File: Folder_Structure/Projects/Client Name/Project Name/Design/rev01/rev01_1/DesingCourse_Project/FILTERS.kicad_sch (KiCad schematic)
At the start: 17 parts, among them J10 874380643

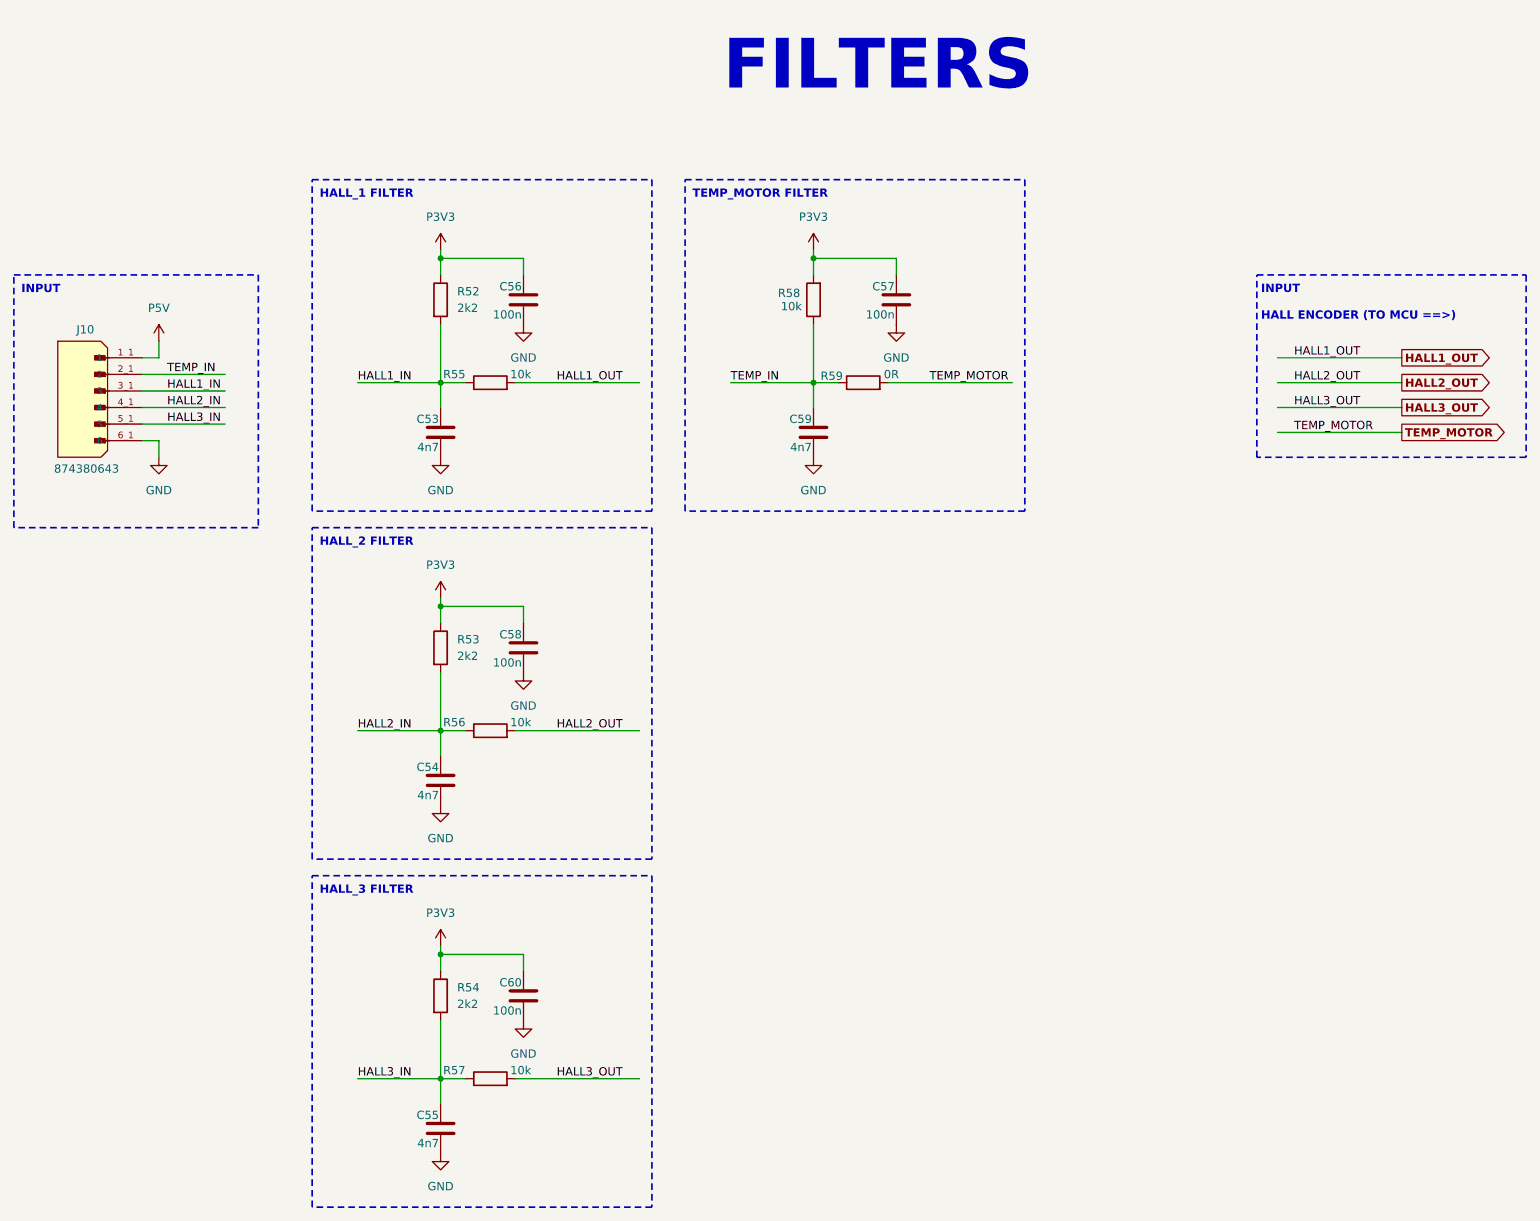
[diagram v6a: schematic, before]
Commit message: Update 16
Initial component placement done
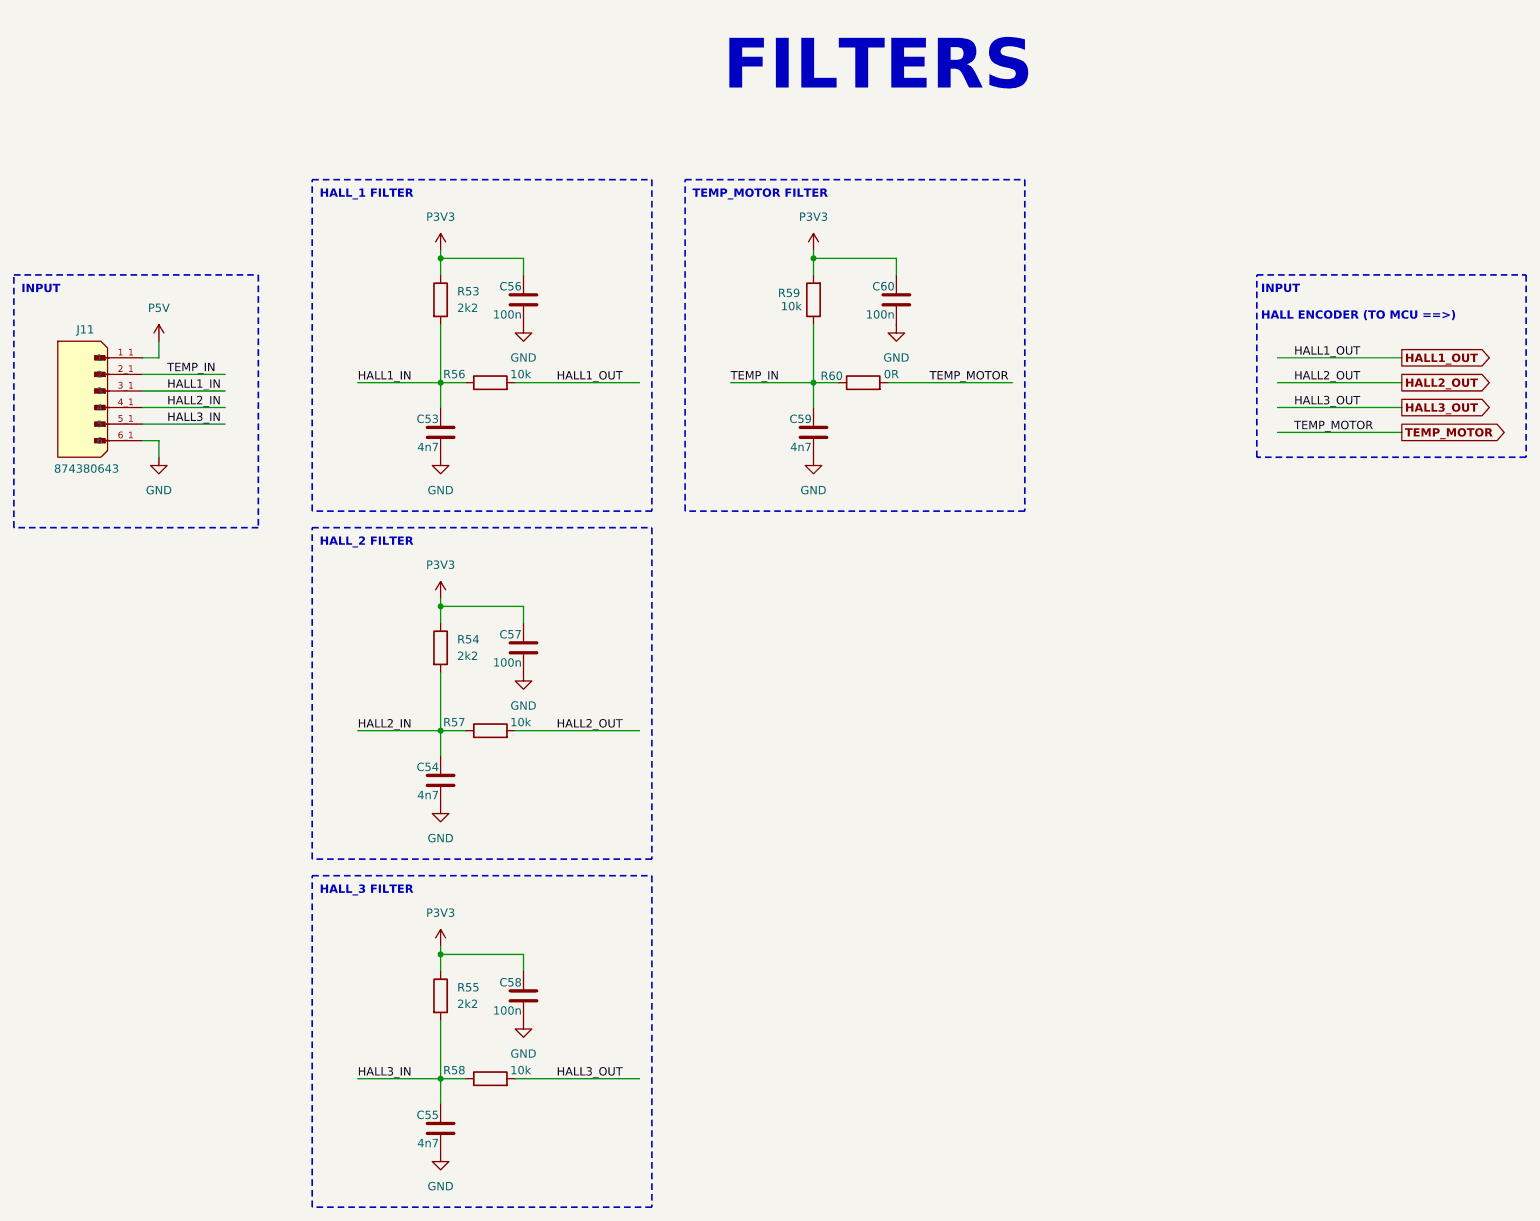
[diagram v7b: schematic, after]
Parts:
- renumbered C58 to C57, C60 to C58, C57 to C60, J10 to J11, R52 to R53, R53 to R54, R54 to R55, R55 to R56, R56 to R57, R57 to R58, R58 to R59, R59 to R60

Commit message: Update18
Layout finished, clean up or layout and designators.
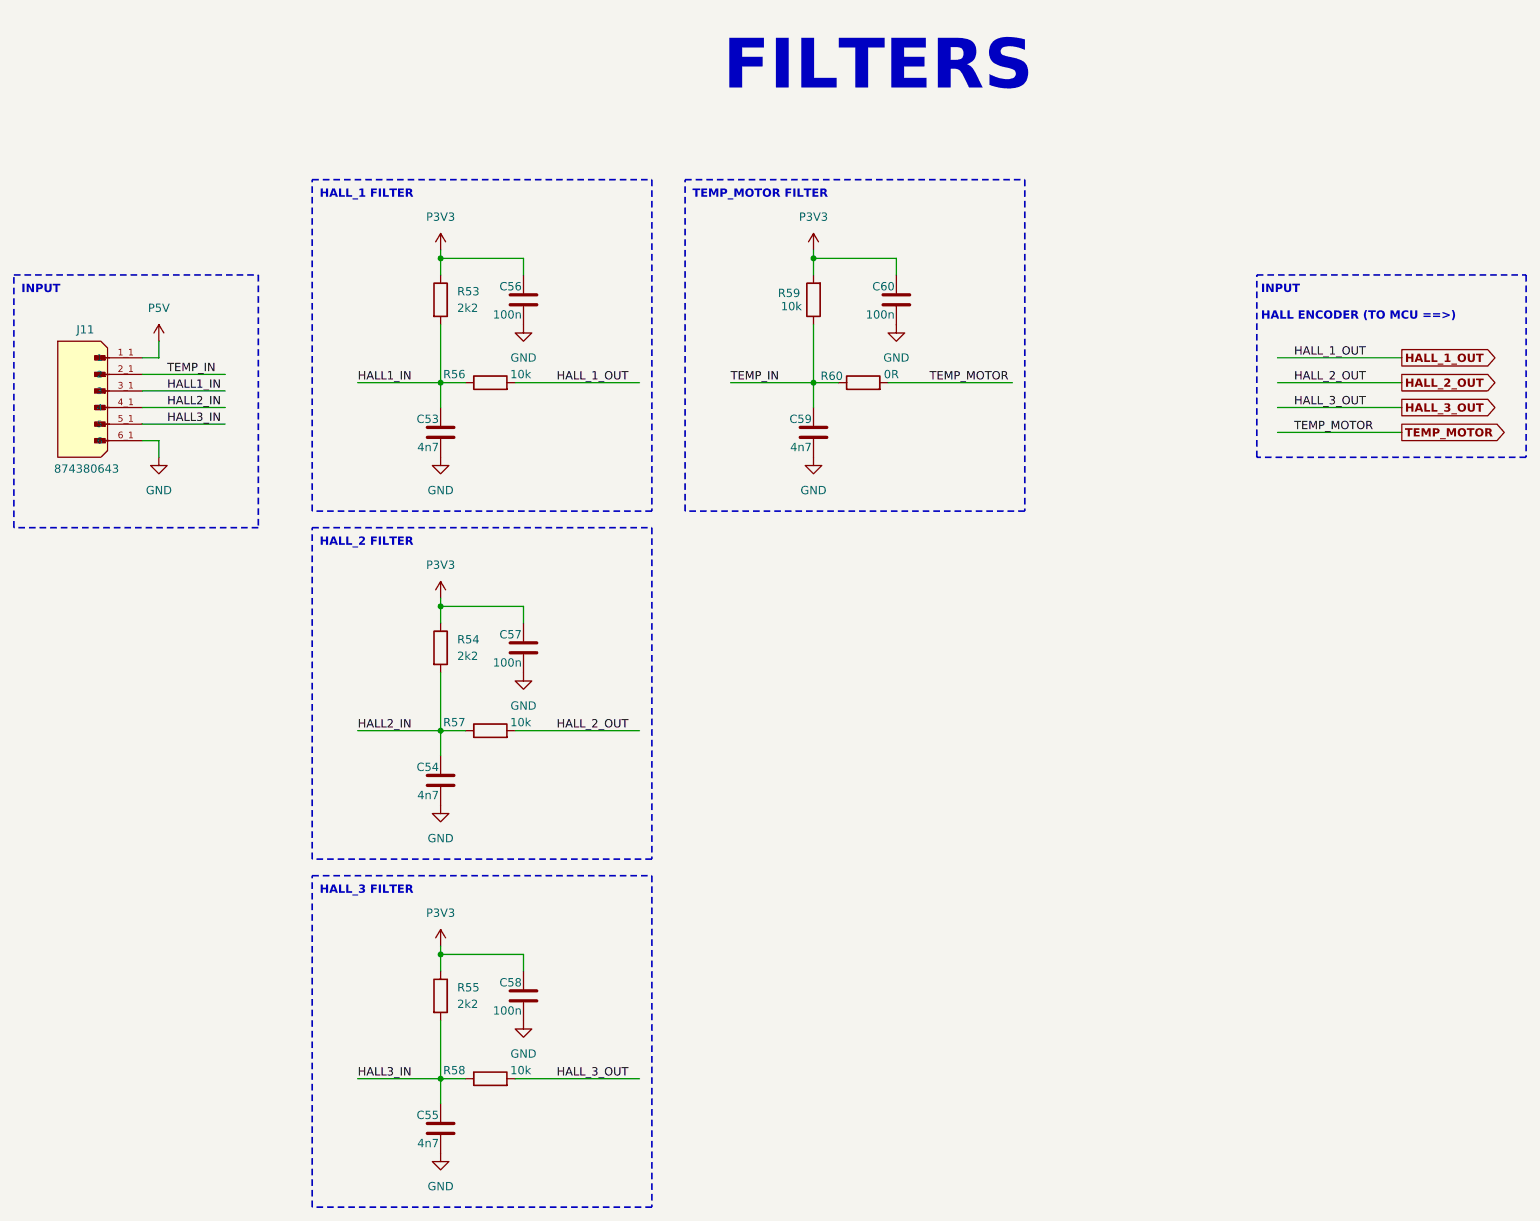
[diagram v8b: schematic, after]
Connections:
- net HALL1_OUT renamed HALL_1_OUT
- net HALL2_OUT renamed HALL_2_OUT
- net HALL3_OUT renamed HALL_3_OUT
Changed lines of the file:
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@@
 		)
 	)
-	(label "HALL3_OUT"
+	(label "HALL_3_OUT"
 		(at 223.52 72.39 0)
 		(effects
@@
 		)
 	)
-	(label "HALL2_OUT"
+	(label "HALL_2_OUT"
 		(at 223.52 68.58 0)
 		(effects
@@
 		)
 	)
-	(label "HALL2_OUT"
+	(label "HALL_2_OUT"
 		(at 110.49 121.92 0)
 		(effects
@@
 		)
 	)
-	(label "HALL3_OUT"
+	(label "HALL_3_OUT"
 		(at 110.49 175.26 0)
 		(effects
@@
 		)
 	)
-	(label "HALL1_OUT"
+	(label "HALL_1_OUT"
 		(at 223.52 64.77 0)
 		(effects
@@
 		)
 	)
-	(label "HALL1_OUT"
+	(label "HALL_1_OUT"
 		(at 110.49 68.58 0)
 		(effects
@@
 		)
 	)
-	(global_label "HALL3_OUT"
+	(global_label "HALL_3_OUT"
 		(shape output)
 		(at 240.03 72.39 0)
@@
 		)
 		(property "Intersheetrefs" "${INTERSHEET_REFS}"
-			(at 253.8673 72.39 0)
+			(at 254.8349 72.39 0)
 			(effects
 				(font
@@
 		)
 	)
-	(global_label "HALL1_OUT"
+	(global_label "HALL_1_OUT"
 		(shape output)
 		(at 240.03 64.77 0)
@@
 		)
 		(property "Intersheetrefs" "${INTERSHEET_REFS}"
-			(at 253.8673 64.77 0)
+			(at 254.8349 64.77 0)
 			(effects
 				(font
@@
 		)
 	)
-	(global_label "HALL2_OUT"
+	(global_label "HALL_2_OUT"
 		(shape output)
 		(at 240.03 68.58 0)
@@
 		)
 		(property "Intersheetrefs" "${INTERSHEET_REFS}"
-			(at 253.8673 68.58 0)
+			(at 254.8349 68.58 0)
 			(effects
 				(font
@@
 			)
 		)
-		(property "Description" "RES 10k OHM 0603 ±1% 1/10W"
+		(property "Description" "Resistor"
 			(at 100.33 121.92 0)
 			(effects
@@
 			)
 		)
-		(property "Description" "RES 2k2 OHM 0603 ±1% 1/10W"
+		(property "Description" "Resistor"
 			(at 92.71 109.22 0)
 			(effects
@@
 			)
 		)
-		(property "Description" "CAP CER 4.7nF 50V X7R 0603"
+		(property "Description" "Unpolarized capacitor"
 			(at 92.71 182.88 0)
 			(effects
@@
 			)
 		)
-		(property "Description" "RES 2k2 OHM 0603 ±1% 1/10W"
+		(property "Description" "Resistor"
 			(at 92.71 55.88 0)
 			(effects
@@
 			)
 		)
-		(property "Description" "CAP CER 0.1UF 10V X7R 0603"
+		(property "Description" "Unpolarized capacitor"
 			(at 162.56 55.88 0)
 			(effects
@@
 			)
 		)
-		(property "Description" "RES 2k2 OHM 0603 ±1% 1/10W"
+		(property "Description" "Resistor"
 			(at 92.71 162.56 0)
 			(effects
@@
 			)
 		)
-		(property "Description" "CAP CER 0.1UF 10V X7R 0603"
+		(property "Description" "Unpolarized capacitor"
 			(at 105.41 109.22 0)
 			(effects
@@
 			)
 		)
-		(property "Description" "RES 10k OHM 0603 ±1% 1/10W"
+		(property "Description" "Resistor"
 			(at 100.33 68.58 0)
 			(effects
@@
 			)
 		)
-		(property "Description" "CAP CER 0.1UF 10V X7R 0603"
+		(property "Description" "Unpolarized capacitor"
 			(at 105.41 55.88 0)
 			(effects
@@
 			)
 		)
-		(property "Description" "CAP CER 4.7nF 50V X7R 0603"
+		(property "Description" "Unpolarized capacitor"
 			(at 92.71 129.54 0)
 			(effects
@@
 			)
 		)
-		(property "Description" "RES 0 OHM 0603 ±1% 1/10W"
+		(property "Description" "Resistor"
 			(at 157.48 68.58 0)
 			(effects
@@
 			)
 		)
-		(property "Description" "RES 10k OHM 0603 ±1% 1/10W"
+		(property "Description" "Resistor"
 			(at 100.33 175.26 0)
 			(effects
@@
 			)
 		)
-		(property "Description" "CAP CER 0.1UF 10V X7R 0603"
+		(property "Description" "Unpolarized capacitor"
 			(at 105.41 162.56 0)
 			(effects
@@
 			)
 		)
-		(property "Description" "CAP CER 4.7nF 50V X7R 0603"
+		(property "Description" "Unpolarized capacitor"
 			(at 149.86 76.2 0)
 			(effects
@@
 			)
 		)
-		(property "Description" "RES 10k OHM 0603 ±1% 1/10W"
+		(property "Description" "Resistor"
 			(at 149.86 55.88 0)
 			(effects
@@
 			)
 		)
-		(property "Description" "CAP CER 4.7nF 50V X7R 0603"
+		(property "Description" "Unpolarized capacitor"
 			(at 92.71 76.2 0)
 			(effects
